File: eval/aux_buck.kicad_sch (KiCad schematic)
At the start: 0 parts

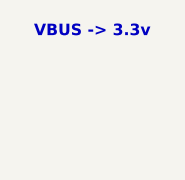
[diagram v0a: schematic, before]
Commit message: Complete most MCU pinout setup
next step power rail and pd
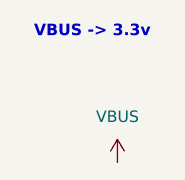
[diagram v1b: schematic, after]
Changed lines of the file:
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@@
+		)
+	)
+	(symbol
+		(lib_id "power:VBUS")
+		(at 45.72 50.8 0)
+		(unit 1)
+		(body_style 1)
+		(exclude_from_sim no)
+		(in_bom yes)
+		(on_board yes)
+		(in_pos_files yes)
+		(dnp no)
+		(fields_autoplaced yes)
+		(property "Reference" "#PWR015"
+			(at 45.72 54.61 0)
+			(hide yes)
+			(show_name no)
+			(do_not_autoplace no)
+			(effects
+				(font
+					(size 1.27 1.27)
+				)
+			)
+		)
+		(property "Value" "VBUS"
+			(at 45.72 45.72 0)
+			(show_name no)
+			(do_not_autoplace no)
+			(effects
+				(font
+					(size 1.27 1.27)
+				)
+			)
+		)
+		(property "Footprint" ""
+			(at 45.72 50.8 0)
+			(hide yes)
+			(show_name no)
+			(do_not_autoplace no)
+			(effects
+				(font
+					(size 1.27 1.27)
+				)
+			)
+		)
+		(property "Datasheet" ""
+			(at 45.72 50.8 0)
+			(hide yes)
+			(show_name no)
+			(do_not_autoplace no)
+			(effects
+				(font
+					(size 1.27 1.27)
+				)
+			)
+		)
+		(property "Description" "Power symbol creates a global label with name \"VBUS\""
+			(at 45.72 50.8 0)
+			(hide yes)
+			(show_name no)
+			(do_not_autoplace no)
+			(effects
+				(font
+					(size 1.27 1.27)
+				)
+			)
+		)
+		(pin "1"
+		)
+		(instances
+			(project "eval"
+				(path "/8b023652-20db-48ce-ad53-bc2d9a4e5dd4/e5450d34-e34e-454c-8387-40410830d96b"
+					(reference "#PWR015")
+					(unit 1)
+				)
+			)
 		)
 	)

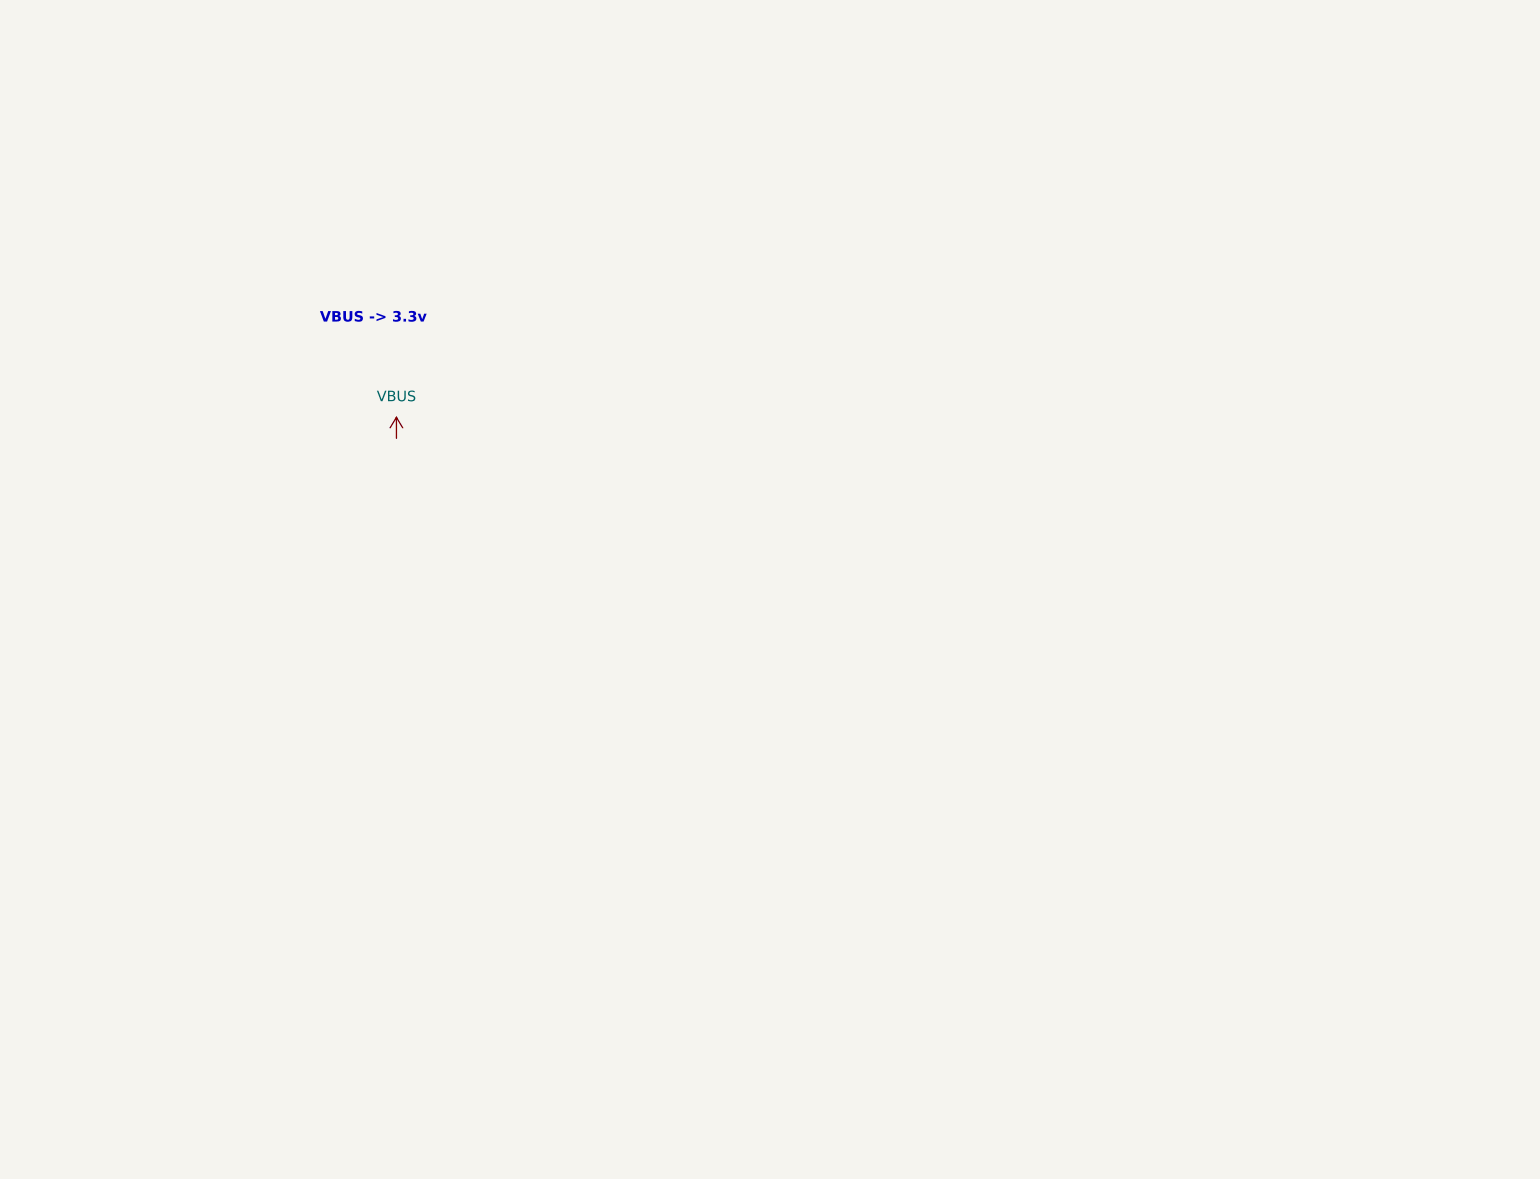
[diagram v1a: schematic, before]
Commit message: complete USB PD, and esd protection
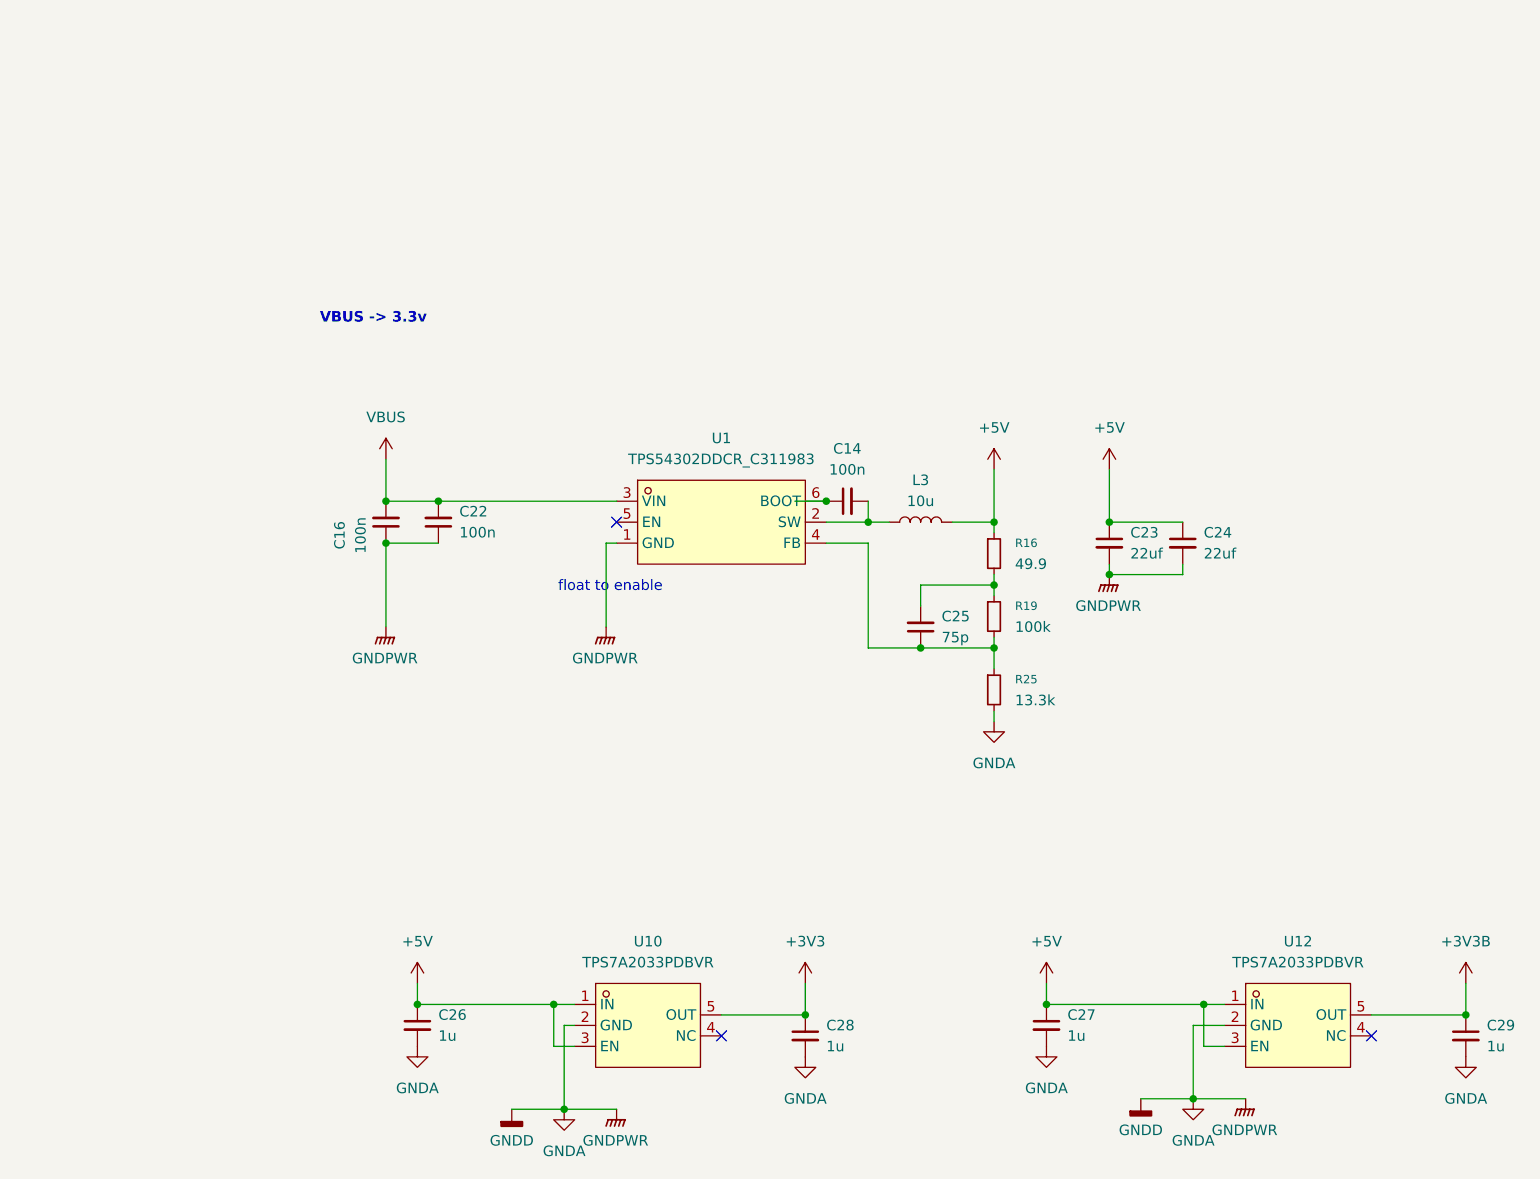
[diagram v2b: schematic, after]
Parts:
- added C14, C16, C22: 100n, symbol Device:C_Small
- added C23, C24: 22uf, symbol Device:C_Small
- added C25: 75p, symbol Device:C_Small
- added C26, C27, C28, C29: 1u, symbol Device:C_Small
- added L3: 10u, symbol Device:L
- added R16: 49.9, symbol Device:R_Small
- added R19: 100k, symbol Device:R_Small
- added R25: 13.3k, symbol Device:R_Small
- added U1: TPS54302DDCR_C311983, EasyEDA:SOT-23-6_L2.9-W1.6-P0.95-LS2.8-BL, symbol EasyEDA:TPS54302DDCR_C311983
- added U10, U12: TPS7A2033PDBVR, EasyEDA:SOT-23-5_L2.9-W1.6-P0.95-LS2.8-BR, symbol EasyEDA:TPS7A2033PDBVR
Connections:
- net VBUS: now also C16.2, C22.2, U1.3 (VIN)
- new net: C25.2, R16.2, R19.1
- new net: C25.1, R19.2, R25.1, U1.4 (FB)
- new net: C14.2, L3.1, U1.2 (SW)
- new net: C14.1, U1.6 (BOOT)
- new net +3V3: C28.1, U10.5 (OUT)
- new net +3V3B: C29.1, U12.5 (OUT)
- new net +5V: C23.1, C24.1, C26.1, C27.1, L3.2, R16.1, U10.1 (IN), U10.3 (EN), U12.1 (IN), U12.3 (EN)
- new net GNDA: C16.1, C22.1, C23.2, C24.2, C26.2, C27.2, C28.2, C29.2, R25.2, U1.1 (GND), U10.2 (GND), U12.2 (GND)
- no-connect marks 0 -> 3
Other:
- note added: "float to enable"

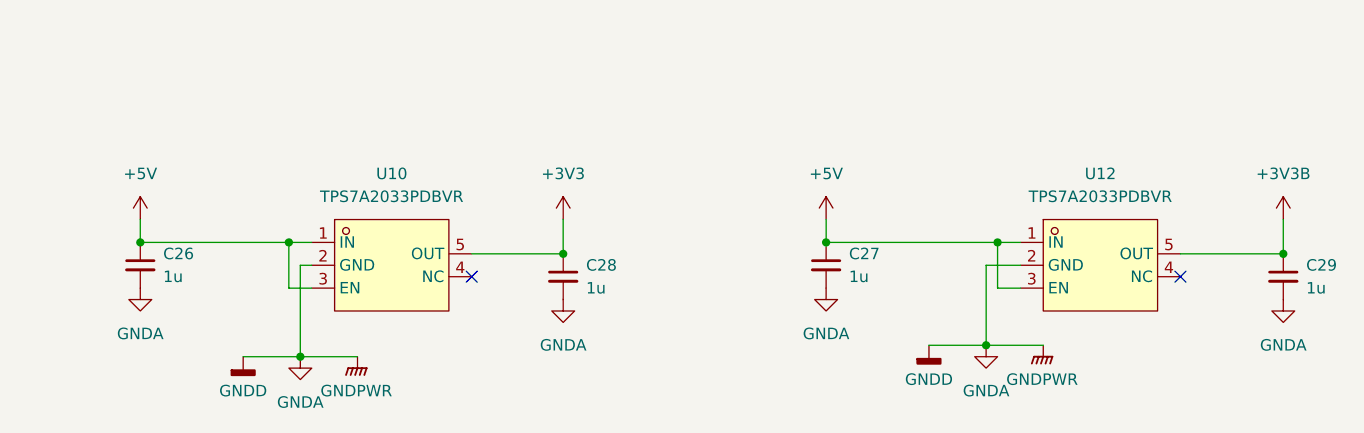
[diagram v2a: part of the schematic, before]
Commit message: Complete first complete draft sch (add screen spi and back light cc)
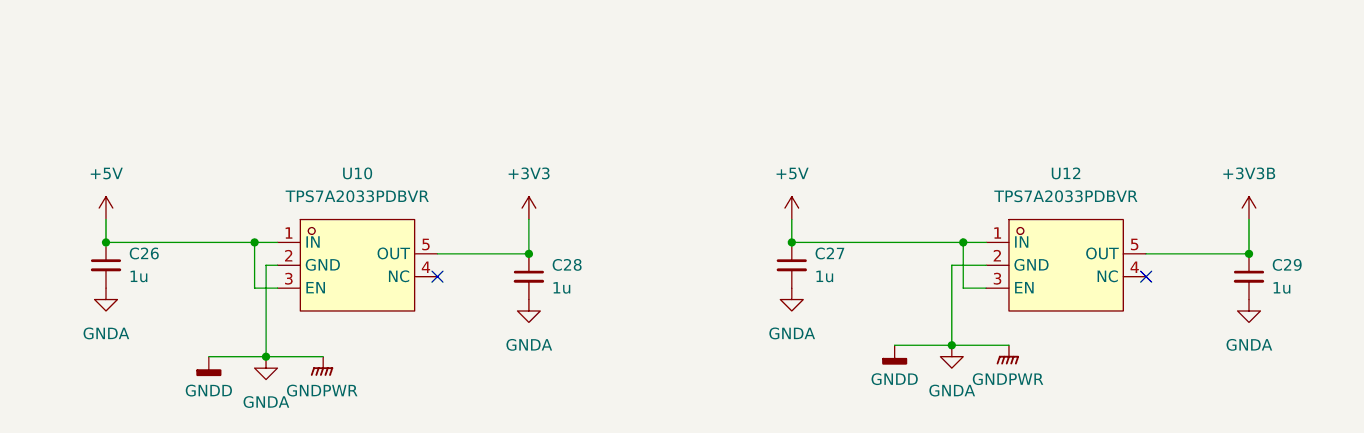
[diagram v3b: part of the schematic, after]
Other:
- moved on the sheet: C26, C27, C28, C29, U10, U12

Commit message: [Layout] complete loop, root and buck layout
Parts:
- C14, C16, C22, C23, C24, C25, C26, C27, C28, C29: footprint (none) -> Capacitor_SMD:C_0603_1608Metric
- R16, R19, R25: footprint (none) -> Resistor_SMD:R_0603_1608Metric
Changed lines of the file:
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@@
 			)
 		)
-		(property "Footprint" ""
+		(property "Footprint" "Capacitor_SMD:C_0603_1608Metric"
 			(at 50.8 60.96 0)
 			(hide yes)
@@
 			)
 		)
-		(property "Footprint" ""
+		(property "Footprint" "Resistor_SMD:R_0603_1608Metric"
 			(at 118.11 72.39 0)
 			(hide yes)
@@
 			)
 		)
-		(property "Footprint" ""
+		(property "Footprint" "Capacitor_SMD:C_0603_1608Metric"
 			(at 120.65 121.92 0)
 			(hide yes)
@@
 			)
 		)
-		(property "Footprint" ""
+		(property "Footprint" "Capacitor_SMD:C_0603_1608Metric"
 			(at 44.45 121.92 0)
 			(hide yes)
@@
 			)
 		)
-		(property "Footprint" ""
+		(property "Footprint" "Resistor_SMD:R_0603_1608Metric"
 			(at 118.11 81.28 0)
 			(hide yes)
@@
 			)
 		)
-		(property "Footprint" ""
+		(property "Footprint" "Capacitor_SMD:C_0603_1608Metric"
 			(at 109.22 73.66 0)
 			(hide yes)
@@
 			)
 		)
-		(property "Footprint" ""
+		(property "Footprint" "Capacitor_SMD:C_0603_1608Metric"
 			(at 100.33 58.42 0)
 			(hide yes)
@@
 			)
 		)
-		(property "Footprint" ""
+		(property "Footprint" "Capacitor_SMD:C_0603_1608Metric"
 			(at 171.45 123.19 0)
 			(hide yes)
@@
 			)
 		)
-		(property "Footprint" ""
+		(property "Footprint" "Capacitor_SMD:C_0603_1608Metric"
 			(at 140.97 63.5 0)
 			(hide yes)
@@
 			)
 		)
-		(property "Footprint" ""
+		(property "Footprint" "Capacitor_SMD:C_0603_1608Metric"
 			(at 91.44 123.19 0)
 			(hide yes)
@@
 			)
 		)
-		(property "Footprint" ""
+		(property "Footprint" "Capacitor_SMD:C_0603_1608Metric"
 			(at 44.45 60.96 0)
 			(hide yes)
@@
 			)
 		)
-		(property "Footprint" ""
+		(property "Footprint" "Resistor_SMD:R_0603_1608Metric"
 			(at 118.11 64.77 0)
 			(hide yes)
@@
 			)
 		)
-		(property "Footprint" ""
+		(property "Footprint" "Capacitor_SMD:C_0603_1608Metric"
 			(at 132.08 63.5 0)
 			(hide yes)

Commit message: [layout] complete for each sub module
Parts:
- removed C24: 22uf, Capacitor_SMD:C_0603_1608Metric, symbol Device:C_Small
- removed L3: 10u, symbol Device:L
- added C44: 47u, EasyEDA:C1206, symbol EasyEDA:HGC1206R5476M100NSPJ
- added L2: FXL0420-100-M, EasyEDA:IND-SMD_L4.4-W4.2, symbol EasyEDA:FXL0420-100-M
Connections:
- net +5V: now also C44.1, L2.2
- net GNDA: now also C44.2
- net at C14.2, U1.2 (SW): now also L2.1

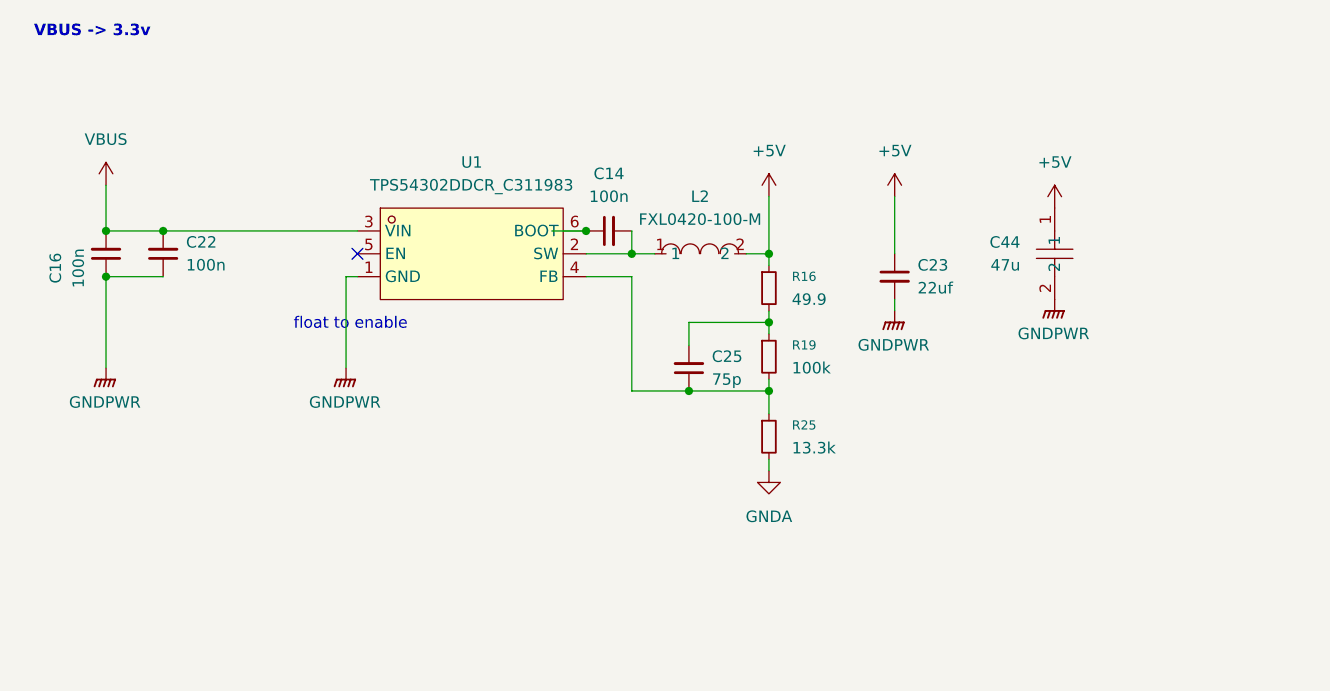
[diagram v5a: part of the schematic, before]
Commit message: [sch] Add ORing for 2 input
plan to add back to back mos protection for output (high side mos)
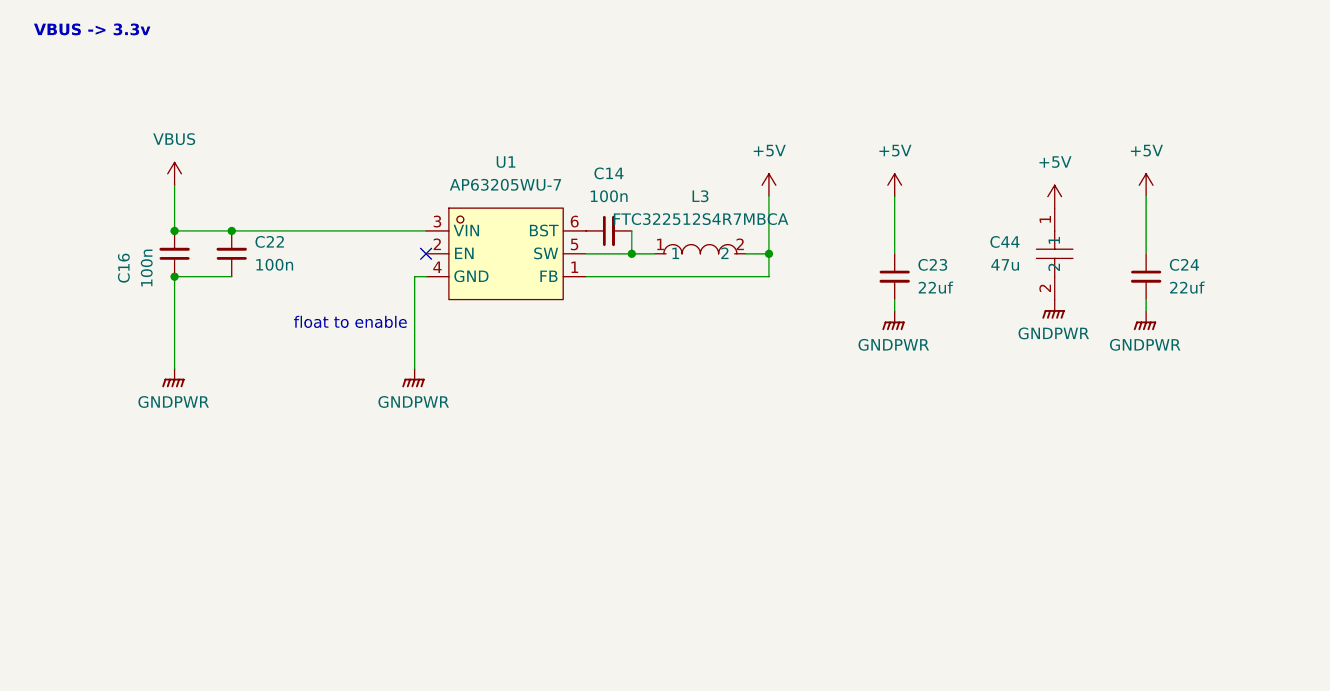
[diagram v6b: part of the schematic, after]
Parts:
- removed C25: 75p, Capacitor_SMD:C_0603_1608Metric, symbol Device:C_Small
- removed L2: FXL0420-100-M, EasyEDA:IND-SMD_L4.4-W4.2, symbol EasyEDA:FXL0420-100-M
- removed R16: 49.9, Resistor_SMD:R_0603_1608Metric, symbol Device:R_Small
- removed R19: 100k, Resistor_SMD:R_0603_1608Metric, symbol Device:R_Small
- removed R25: 13.3k, Resistor_SMD:R_0603_1608Metric, symbol Device:R_Small
- removed U1: TPS54302DDCR_C311983, EasyEDA:SOT-23-6_L2.9-W1.6-P0.95-LS2.8-BL, symbol EasyEDA:TPS54302DDCR_C311983
- added C24: 22uf, Capacitor_SMD:C_0603_1608Metric, symbol Device:C_Small
- added L3: FTC322512S4R7MBCA, EasyEDA:IND-SMD_L3.2-W2.5_FTC322520S, symbol EasyEDA:FTC322512S4R7MBCA
- added U1: AP63205WU-7, EasyEDA:TSOT-23-6_L2.9-W1.6-P0.95-LS2.8-BL, symbol EasyEDA:AP63205WU-7
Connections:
- net +5V: now also C24.1, L3.2, U1.1 (FB)
- net GNDA: now also C24.2, U1.4 (GND)
- net VBUS: now also U1.3 (VIN)
- net at C14.2: now also L3.1, U1.5 (SW)
- net at C14.1: now also U1.6 (BST)
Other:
- moved on the sheet: C16, C22
